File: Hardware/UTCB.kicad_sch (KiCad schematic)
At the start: 10 parts, among them J10 Conn_01x06, J9 Conn_01x02

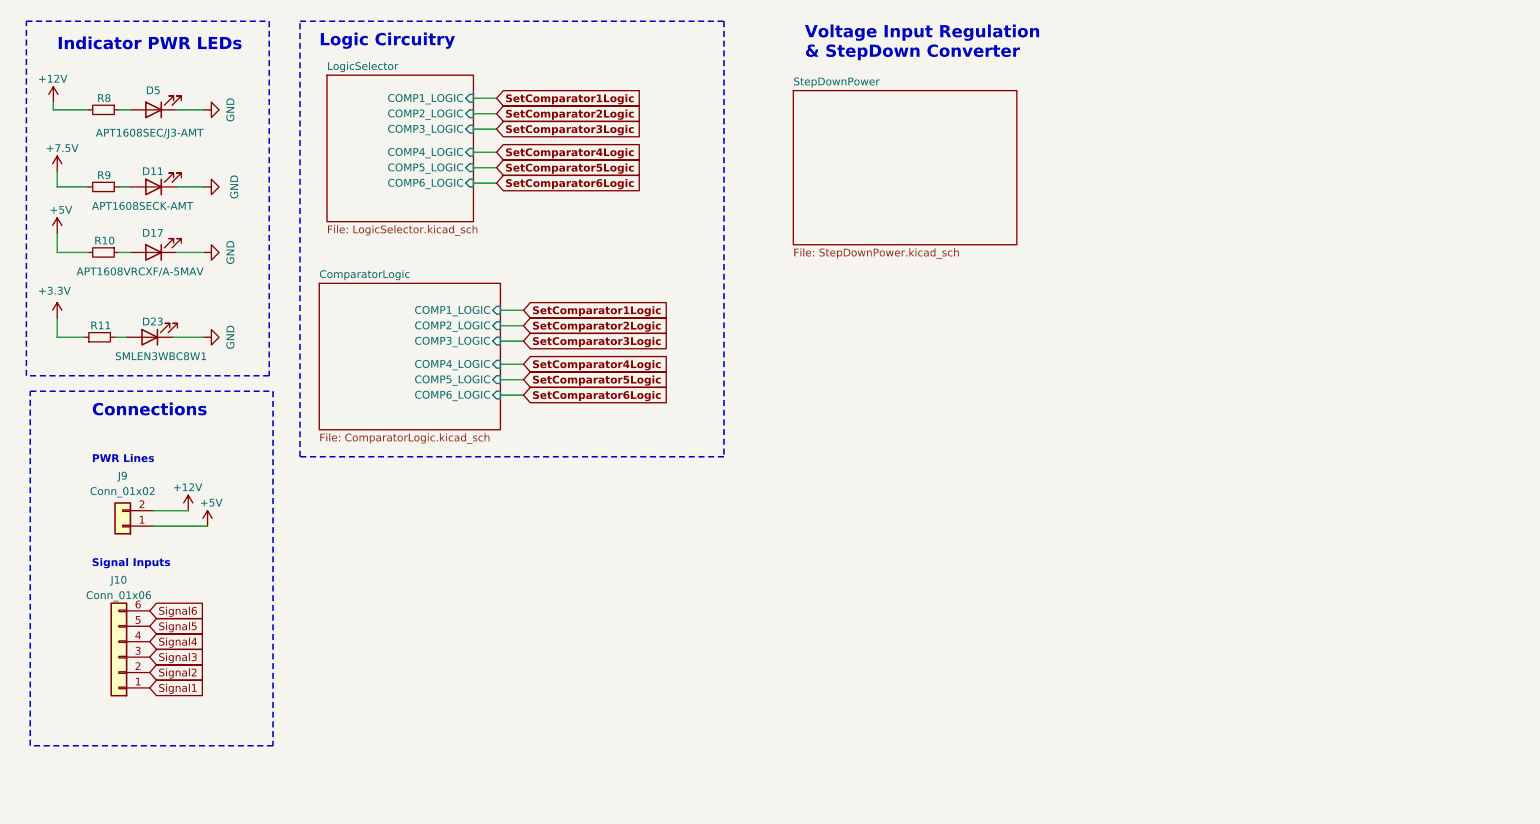
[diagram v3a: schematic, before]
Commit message: Added changes to logic side for comparator inputs
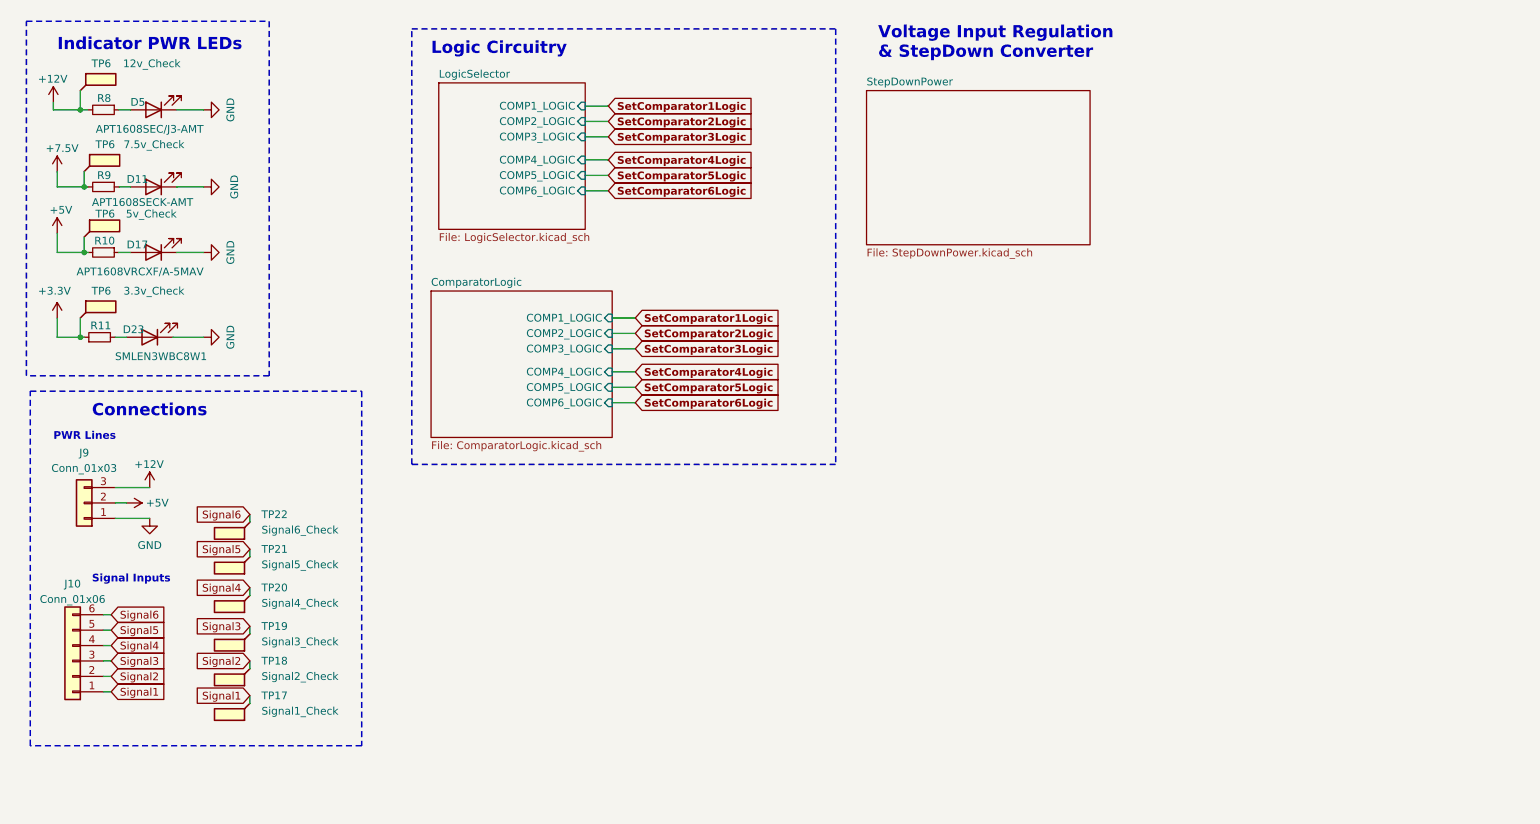
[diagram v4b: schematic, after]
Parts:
- removed J9: Conn_01x02, Connector_PinHeader_1.27mm:PinHeader_1x02_P1.27mm_Vertical, symbol Connector_Generic:Conn_01x02
- added J9: Conn_01x03, Connector_PinHeader_1.27mm:PinHeader_1x03_P1.27mm_Vertical, symbol Connector_Generic:Conn_01x03
- added TP17: Signal1_Check, TestPoint:TestPoint_Keystone_5015_Micro-Minature, symbol Connector:TestPoint_Flag
- added TP18: Signal2_Check, TestPoint:TestPoint_Keystone_5015_Micro-Minature, symbol Connector:TestPoint_Flag
- added TP19: Signal3_Check, TestPoint:TestPoint_Keystone_5015_Micro-Minature, symbol Connector:TestPoint_Flag
- added TP20: Signal4_Check, TestPoint:TestPoint_Keystone_5015_Micro-Minature, symbol Connector:TestPoint_Flag
- added TP21: Signal5_Check, TestPoint:TestPoint_Keystone_5015_Micro-Minature, symbol Connector:TestPoint_Flag
- added TP22: Signal6_Check, TestPoint:TestPoint_Keystone_5015_Micro-Minature, symbol Connector:TestPoint_Flag
- added TP6: 5v_Check, TestPoint:TestPoint_Keystone_5015_Micro-Minature, symbol Connector:TestPoint_Flag
- added TP6: 7.5v_Check, TestPoint:TestPoint_Keystone_5015_Micro-Minature, symbol Connector:TestPoint_Flag
- added TP6: 12v_Check, TestPoint:TestPoint_Keystone_5015_Micro-Minature, symbol Connector:TestPoint_Flag
- added TP6: 3.3v_Check, TestPoint:TestPoint_Keystone_5015_Micro-Minature, symbol Connector:TestPoint_Flag
- J10: footprint Connector_PinHeader_1.27mm:PinHeader_1x06_P1.27mm_Vertical -> Connector_PinHeader_1.27mm:PinHeader_1x06_P1.27mm_Horizontal
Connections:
- net +12V: now also J9.3 (Pin_3), TP6.1
- net +3.3V: now also TP6.1
- net +5V: now also J9.2 (Pin_2), TP6.1
- net +7.5V: now also TP6.1
- net GND: now also J9.1 (Pin_1)
- net Signal1: now also TP17.1
- net Signal2: now also TP18.1
- net Signal3: now also TP19.1
- net Signal4: now also TP20.1
- net Signal5: now also TP21.1
- net Signal6: now also TP22.1
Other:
- moved on the sheet: J10

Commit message: Removed a lot of unnecessary BJT logic, removed rotary switches for logic setting (set all to universal final 3.3v based logic)
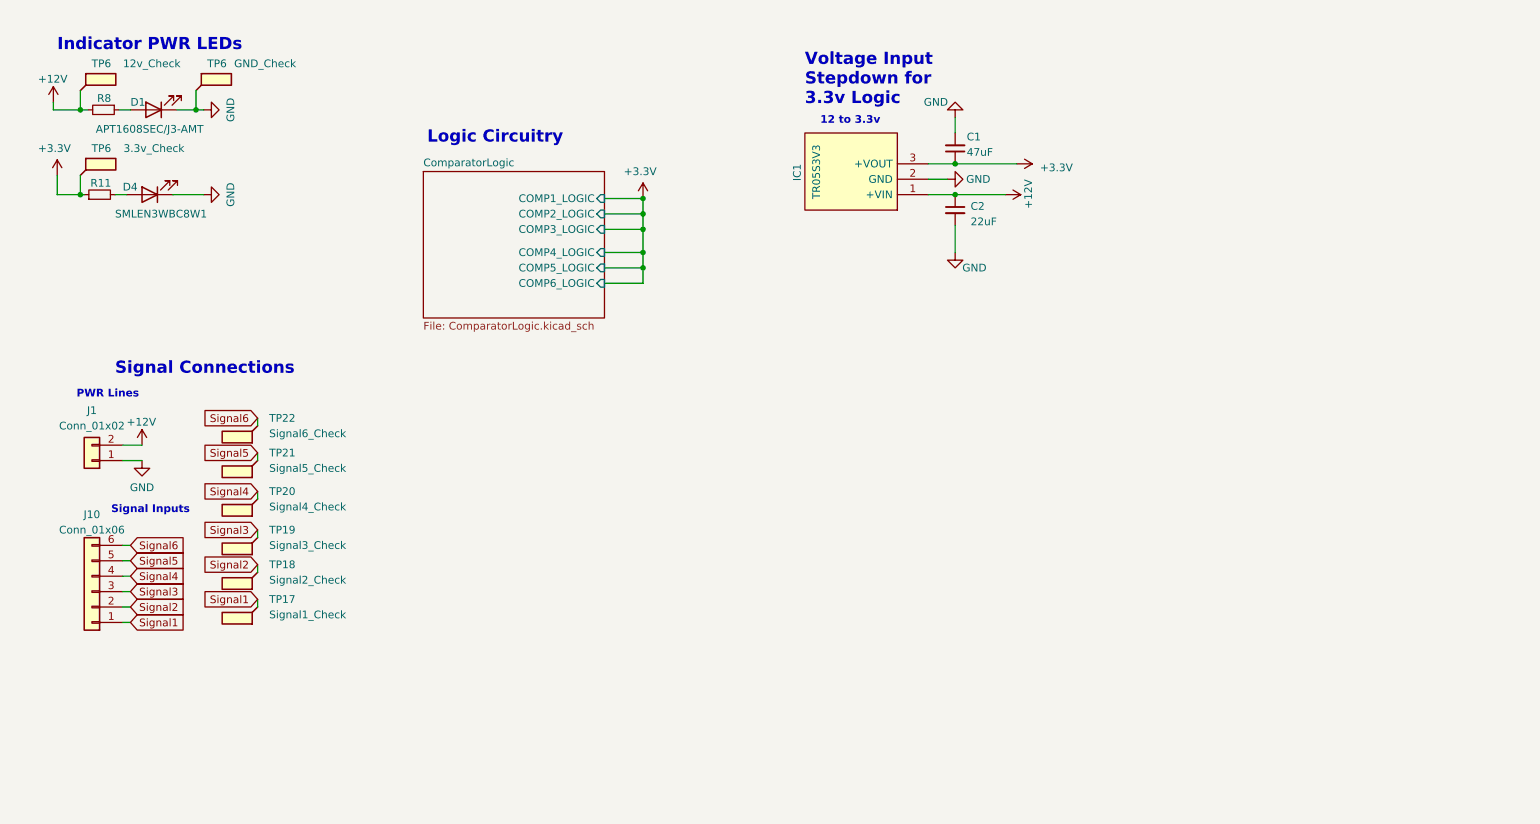
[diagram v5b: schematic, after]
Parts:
- removed D11: APT1608SECK-AMT, Diode_SMD:D_0603_1608Metric, symbol Device:LED
- removed D17: APT1608VRCXF/A-5MAV, Diode_SMD:D_0603_1608Metric, symbol Device:LED
- removed J9: Conn_01x03, Connector_PinHeader_1.27mm:PinHeader_1x03_P1.27mm_Vertical, symbol Connector_Generic:Conn_01x03
- removed R10, R9: R_Small, Resistor_SMD:R_0603_1608Metric, symbol Device:R_Small
- removed TP6: 5v_Check, TestPoint:TestPoint_Keystone_5015_Micro-Minature, symbol Connector:TestPoint_Flag
- removed TP6: 7.5v_Check, TestPoint:TestPoint_Keystone_5015_Micro-Minature, symbol Connector:TestPoint_Flag
- added C1: 47uF, Capacitor_SMD:C_0603_1608Metric, symbol Device:C_Small
- added C2: 22uF, Capacitor_SMD:C_0603_1608Metric, symbol Device:C_Small
- added IC1: TR05S3V3, Converter_DCDC:TR05S3V3, symbol Converter_DCDC:TR05S3V3
- added J1: Conn_01x02, Connector_PinSocket_2.54mm:PinSocket_1x02_P2.54mm_Vertical, symbol Connector_Generic:Conn_01x02
- added TP6: GND_Check, TestPoint:TestPoint_Keystone_5015_Micro-Minature, symbol Connector:TestPoint_Flag
- J10: footprint Connector_PinHeader_1.27mm:PinHeader_1x06_P1.27mm_Horizontal -> Connector_PinHeader_1.27mm:PinHeader_1x06_P1.27mm_Vertical
- renumbered D5 to D1, D23 to D4
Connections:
- net +12V: now also C2.1, IC1.1 (+VIN), J1.2 (Pin_2)
- net +3.3V: now also C1.1, IC1.3 (+VOUT)
- net GND: now also C1.2, C2.2, IC1.2 (GND), J1.1 (Pin_1), TP6.1
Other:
- removed sheet LogicSelector
- removed sheet StepDownPower
- note added: "12 to 3.3v"
- note added: "Signal Connections"
- note added: "Voltage Input Stepdown for 3.3v Logic"
- note removed: "Connections"
- note removed: "Voltage Input Regulation & StepDown Converter"
- moved on the sheet: D4, J10, R11, TP17, TP18, TP19, TP20, TP21, TP22, TP6

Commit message: Organized main sheet
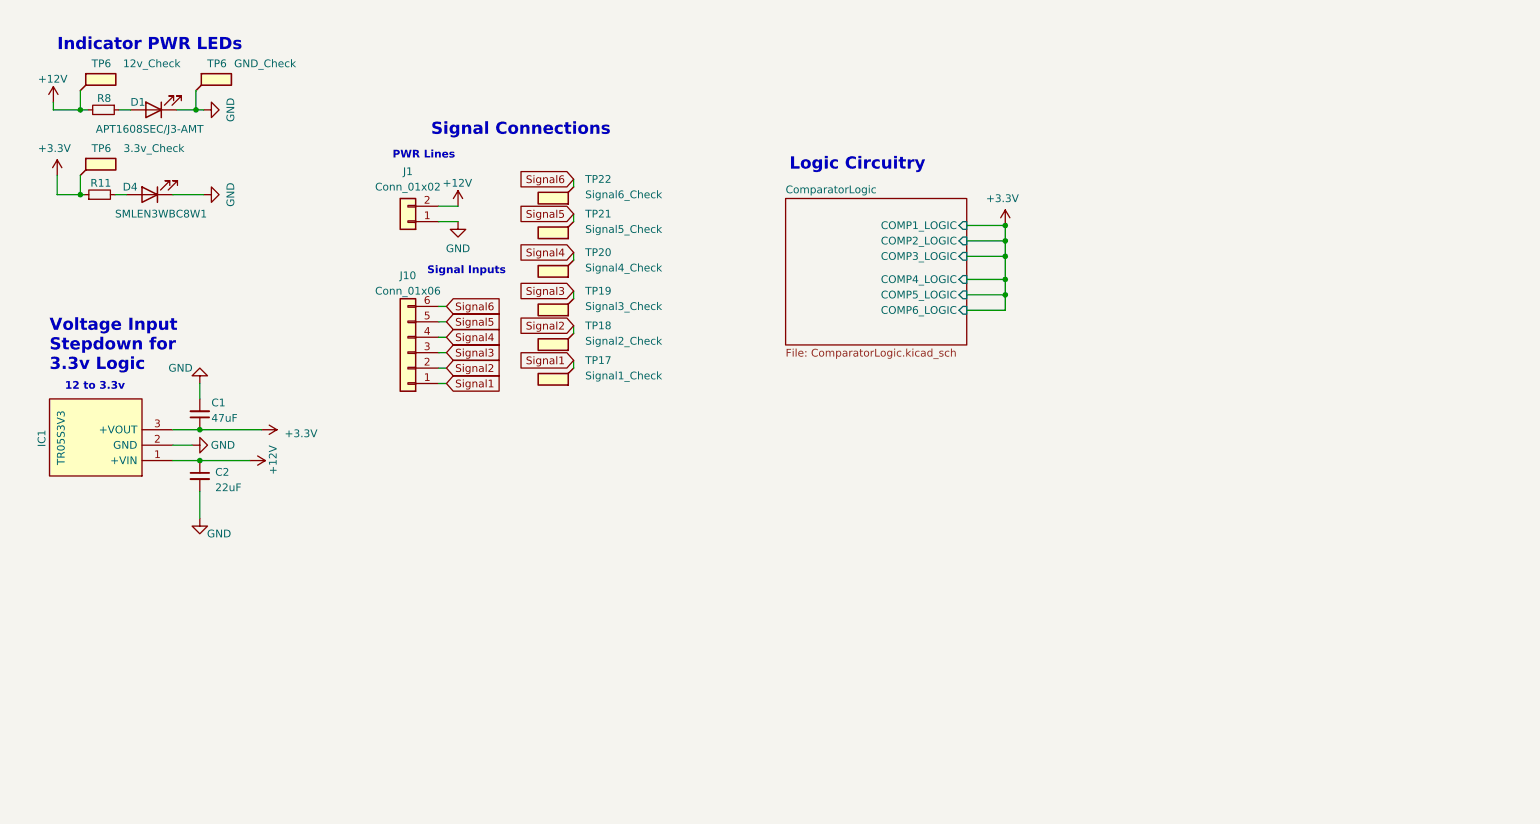
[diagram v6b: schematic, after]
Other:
- moved on the sheet: C1, C2, IC1, J1, J10, TP17, TP18, TP19, TP20, TP21, TP22

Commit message: Minor modifications
Added 3D model for the regulator, updated to socket for signal inputs, and updated to power pours for certain PWR pins.
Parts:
- J10: footprint Connector_PinHeader_1.27mm:PinHeader_1x06_P1.27mm_Vertical -> Connector_PinSocket_1.27mm:PinSocket_1x06_P1.27mm_Vertical
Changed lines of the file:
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@@
       (effects (font (size 1.27 1.27)))
     )
-    (property "Footprint" "Connector_PinHeader_1.27mm:PinHeader_1x06_P1.27mm_Vertical" (at 80.01 69.85 0)
+    (property "Footprint" "Connector_PinSocket_1.27mm:PinSocket_1x06_P1.27mm_Vertical" (at 80.01 69.85 0)
       (effects (font (size 1.27 1.27)) hide)
     )
